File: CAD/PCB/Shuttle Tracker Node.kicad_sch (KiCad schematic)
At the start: 14 parts, among them SW1 SW_Push, SW10 SW_Push, SW11 SW_Push, SW12 SW_Push, SW13 PEC11-4215F-S24, SW2 SW_Push, SW3 SW_Push, SW4 SW_Push, SW5 SW_Push, SW6 SW_Push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

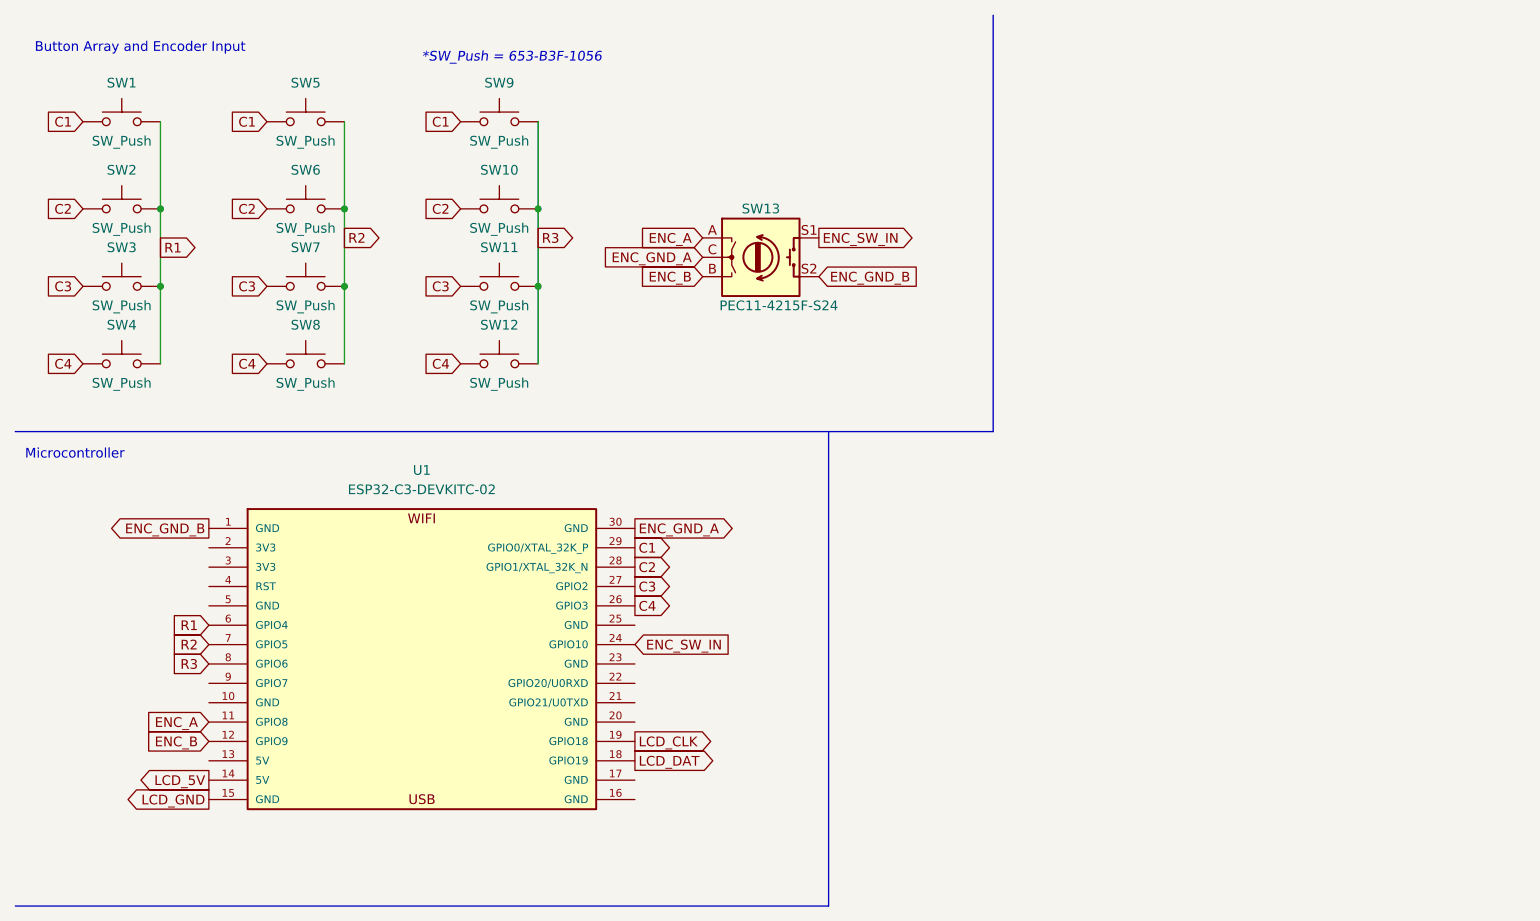
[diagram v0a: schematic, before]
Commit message: Finished PCB Schematic
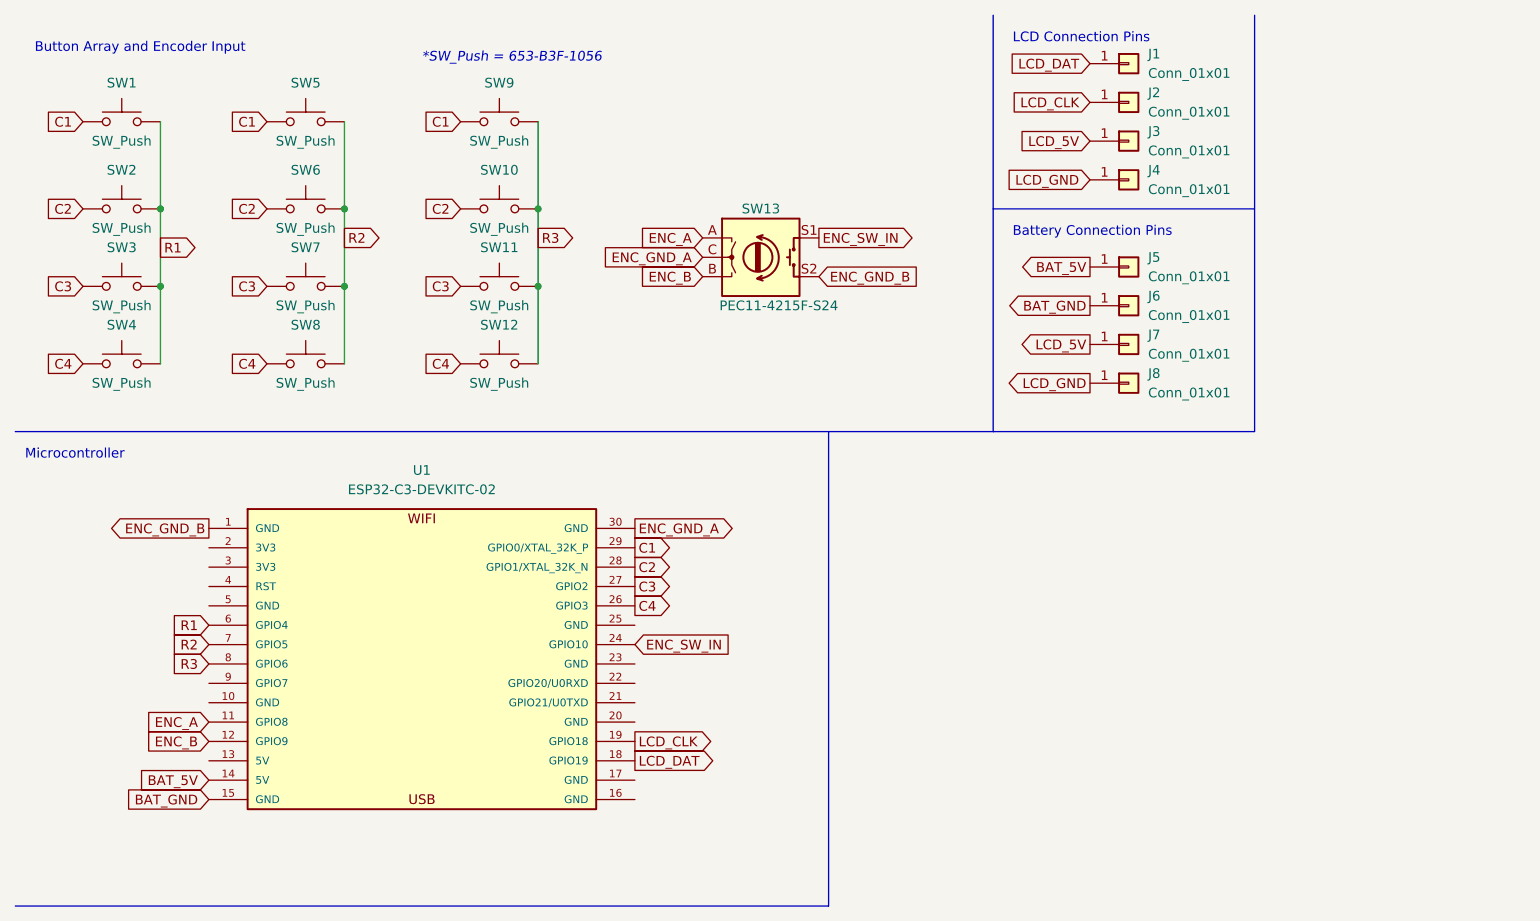
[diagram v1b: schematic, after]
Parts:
- added J1, J2, J3, J4, J5, J6, J7, J8: Conn_01x01, Connector_Pin:Pin_D1.0mm_L10.0mm, symbol Connector_Generic:Conn_01x01
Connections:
- net LCD_5V: now also J3.1 (Pin_1), J7.1 (Pin_1); no longer U1.14 (5V)
- net LCD_CLK: now also J2.1 (Pin_1)
- net LCD_DAT: now also J1.1 (Pin_1)
- net LCD_GND: now also J4.1 (Pin_1), J8.1 (Pin_1); no longer U1.15 (GND)
- new net BAT_5V: J5.1 (Pin_1), U1.14 (5V)
- new net BAT_GND: J6.1 (Pin_1), U1.15 (GND)
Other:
- note added: "Battery Connection Pins"
- note added: "LCD Connection Pins"

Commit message: Place Components on PCB
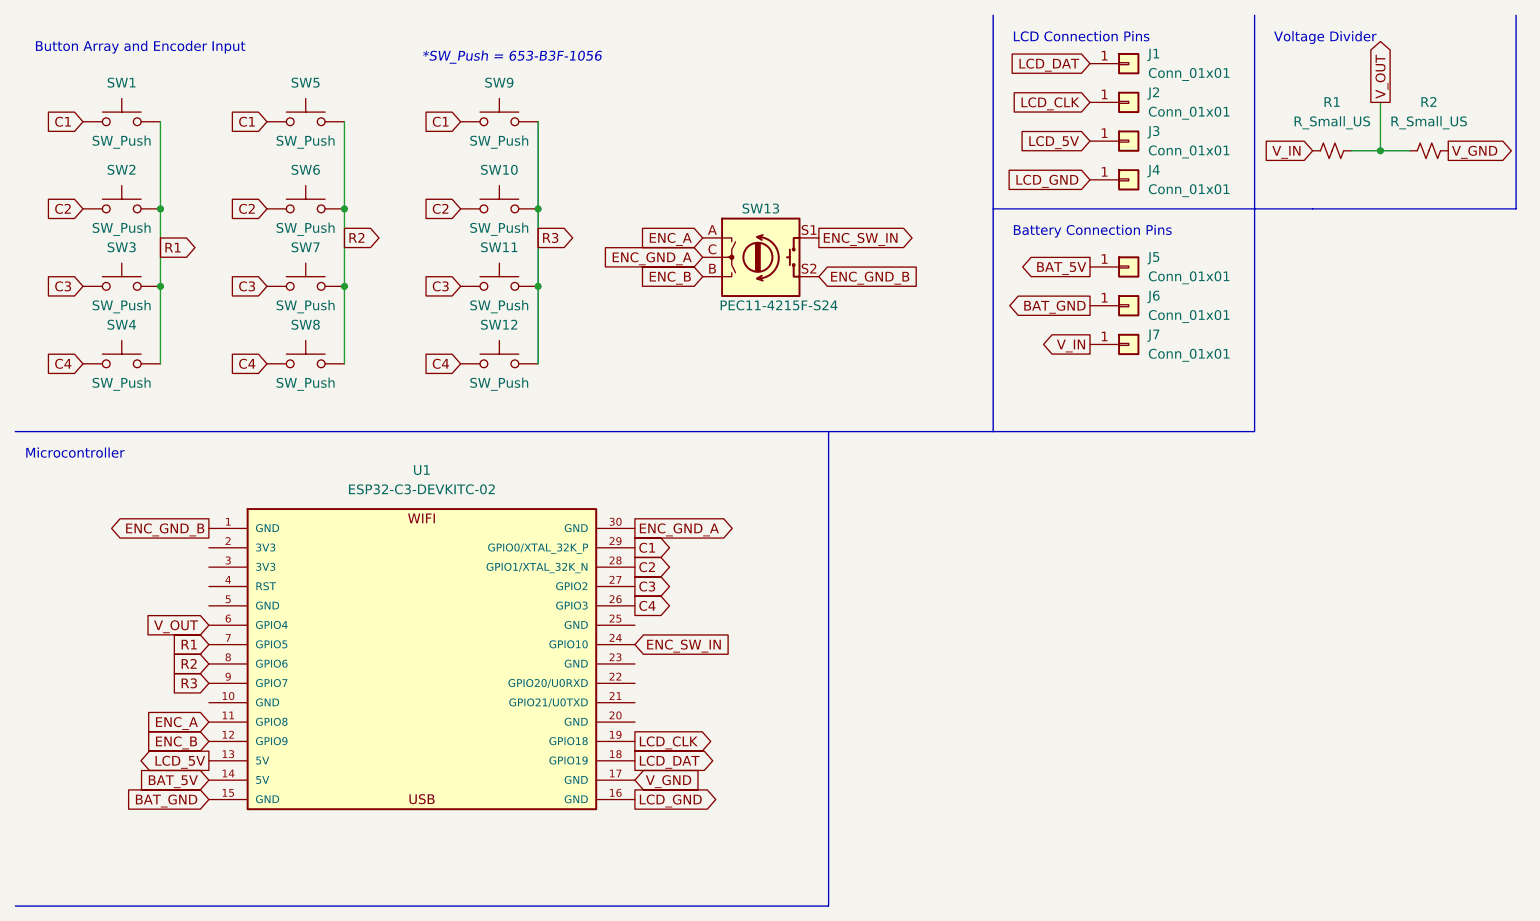
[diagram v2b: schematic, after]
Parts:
- removed J8: Conn_01x01, Connector_Pin:Pin_D1.0mm_L10.0mm, symbol Connector_Generic:Conn_01x01
- added R1, R2: R_Small_US, Resistor_THT:R_Axial_DIN0204_L3.6mm_D1.6mm_P5.08mm_Horizontal, symbol Device:R_Small_US
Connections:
- net LCD_5V: now also U1.13 (5V); no longer J7.1 (Pin_1)
- net LCD_GND: now also U1.16 (GND)
- net R1: now also U1.7 (GPIO5); no longer U1.6 (GPIO4)
- net R2: now also U1.8 (GPIO6); no longer U1.7 (GPIO5)
- net R3: now also U1.9 (GPIO7); no longer U1.8 (GPIO6)
- net V_GND: now reaches U1.17 (GND)
- net V_GND: now also R2.2
- new net V_IN: J7.1 (Pin_1), R1.1
- new net V_OUT: R1.2, R2.1, U1.6 (GPIO4)
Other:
- note added: "Voltage Divider"

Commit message: Finished PCB Routing
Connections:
- net C1: now also U1.26 (GPIO3); no longer U1.29 (GPIO0/XTAL_32K_P)
- net C2: now also U1.27 (GPIO2); no longer U1.28 (GPIO1/XTAL_32K_N)
- net C3: now also U1.28 (GPIO1/XTAL_32K_N); no longer U1.27 (GPIO2)
- net C4: now also U1.29 (GPIO0/XTAL_32K_P); no longer U1.26 (GPIO3)
- net ENC_A: now also U1.12 (GPIO9); no longer U1.11 (GPIO8)
- net ENC_B: now also U1.11 (GPIO8); no longer U1.12 (GPIO9)

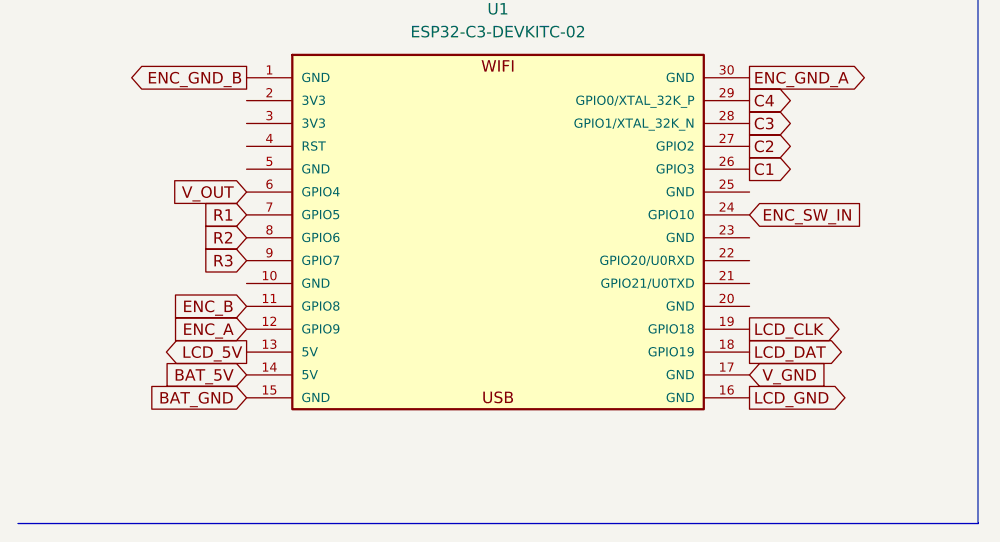
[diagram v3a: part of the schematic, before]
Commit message: Changed IO Configuration
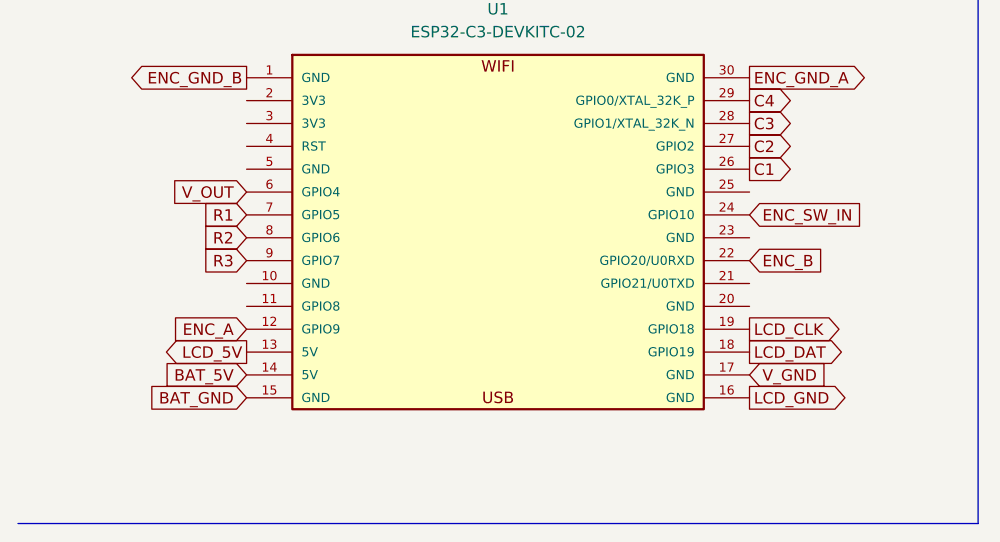
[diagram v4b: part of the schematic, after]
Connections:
- net ENC_B: now also U1.22 (GPIO20/U0RXD); no longer U1.11 (GPIO8)
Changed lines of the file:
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@@
     )
   )
-  (global_label "ENC_B" (shape input) (at 36.83 104.14 180) (fields_autoplaced)
-    (effects (font (size 1.27 1.27)) (justify right))
-    (property "Intersheet References" "${INTERSHEET_REFS}" (id 0) (at 28.4298 104.0606 0)
-      (effects (font (size 1.27 1.27)) (justify right) hide)
+  (global_label "ENC_B" (shape input) (at 92.71 99.06 0) (fields_autoplaced)
+    (effects (font (size 1.27 1.27)) (justify left))
+    (property "Intersheet References" "${INTERSHEET_REFS}" (id 0) (at 101.1102 99.1394 0)
+      (effects (font (size 1.27 1.27)) (justify left) hide)
     )
   )
